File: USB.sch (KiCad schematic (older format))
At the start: 31 parts

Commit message: First version of schematics
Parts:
- added C30, C31, C33, C40, C41: 4u7, symbol device:C_Small
- added C34, C35, C36: 100n, symbol device:C_Small
- added C37, C38: 470u/6.3V, symbol device:CP_Small
- added C39: 1u, symbol device:C_Small
- added C42, C43: 22p, symbol device:C_Small
- added J4: Headphones, symbol conn:Audio-Jack-3
- added J5: Mic, symbol conn:Audio-Jack-3
- added R29: 1k5, symbol device:R_Small
- added R30, R31: 22, symbol device:R_Small
- added R32: 2k2, symbol device:R_Small
- added R33: 1k2, symbol device:R_Small
- added R34: 1M, symbol device:R_Small
- added U8: CM108, symbol GiantKnob:CM108
- added Y3: 12 MHz, symbol device:Crystal_Small
- gave numbers to parts that had none: 31
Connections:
- net +5V: now also C30.1, C31.1, C34.1, C35.1, C36.1, U8.29 (AVDD1), U8.34 (AVDD2), U8.35 (DVDD), U8.7 (PWRSEL)
- net GND: now also C30.2, C31.2, C33.1, C34.2, C35.2, C36.2, C40.2, C41.2, C42.1, C43.1, J4.3, J5.3, U8.10 (MODE), U8.14 (DVSS1), U8.16 (SDIN), U8.22 (ADSEL), U8.23 (TEST), U8.24 (AVSS1), U8.28 (VSEL), U8.33 (AVSS2), U8.36 (DVSS2), U8.38 (MSEL)
- net USBDM_AUDIO: now also R30.2
- net USBDP_AUDIO: now also R29.1, R31.2
- new net: R32.1, U8.25 (VBIAS)
- new net: C40.1, U8.26 (VREF)
- new net: C39.2, U8.27 (MICIN)
- new net: C38.1, U8.30 (LOL)
- new net: C37.1, U8.32 (LOR)
- new net: C33.2, R29.2, U8.37 (REGV)
- new net: R31.1, U8.41 (USBDP)
- new net: R30.1, U8.42 (USBDM)
- new net: C42.2, R34.1, U8.8 (XI), Y3.1
- new net: C43.2, R34.2, U8.9 (XO), Y3.2
- new net: C41.1, R32.2, R33.1
- new net: J5.2, R33.2
- new net: C39.1, J5.1
- new net: C38.2, J4.1
- new net: C37.2, J4.2
- no-connect marks 13 -> 37

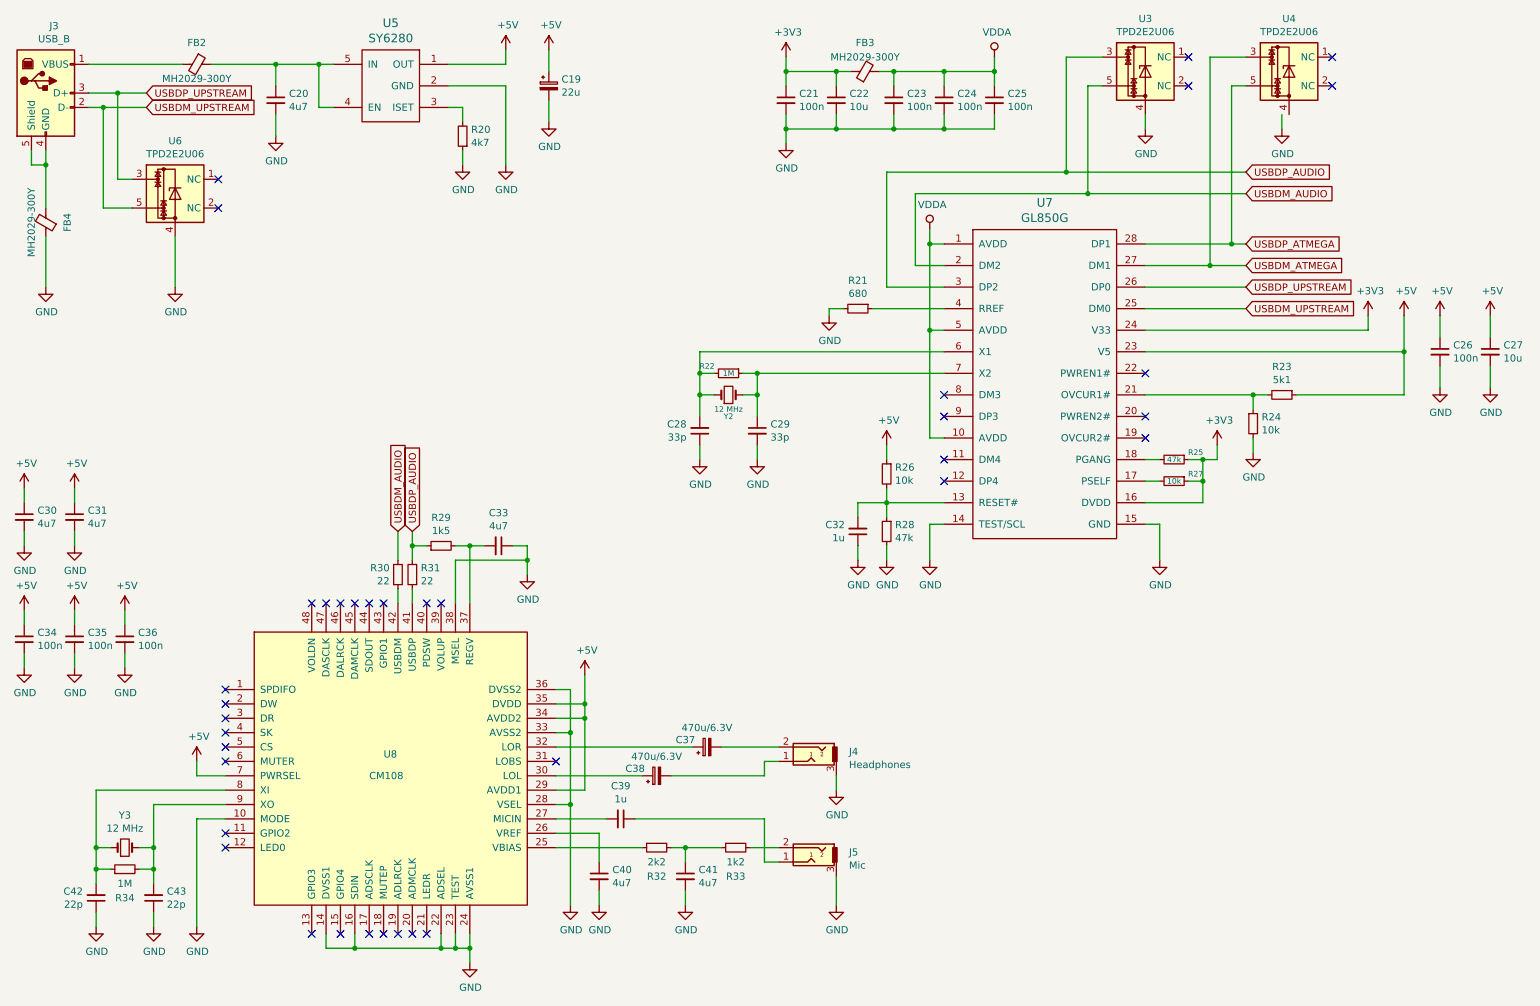
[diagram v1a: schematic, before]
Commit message: Added PTT to ATmega32U4
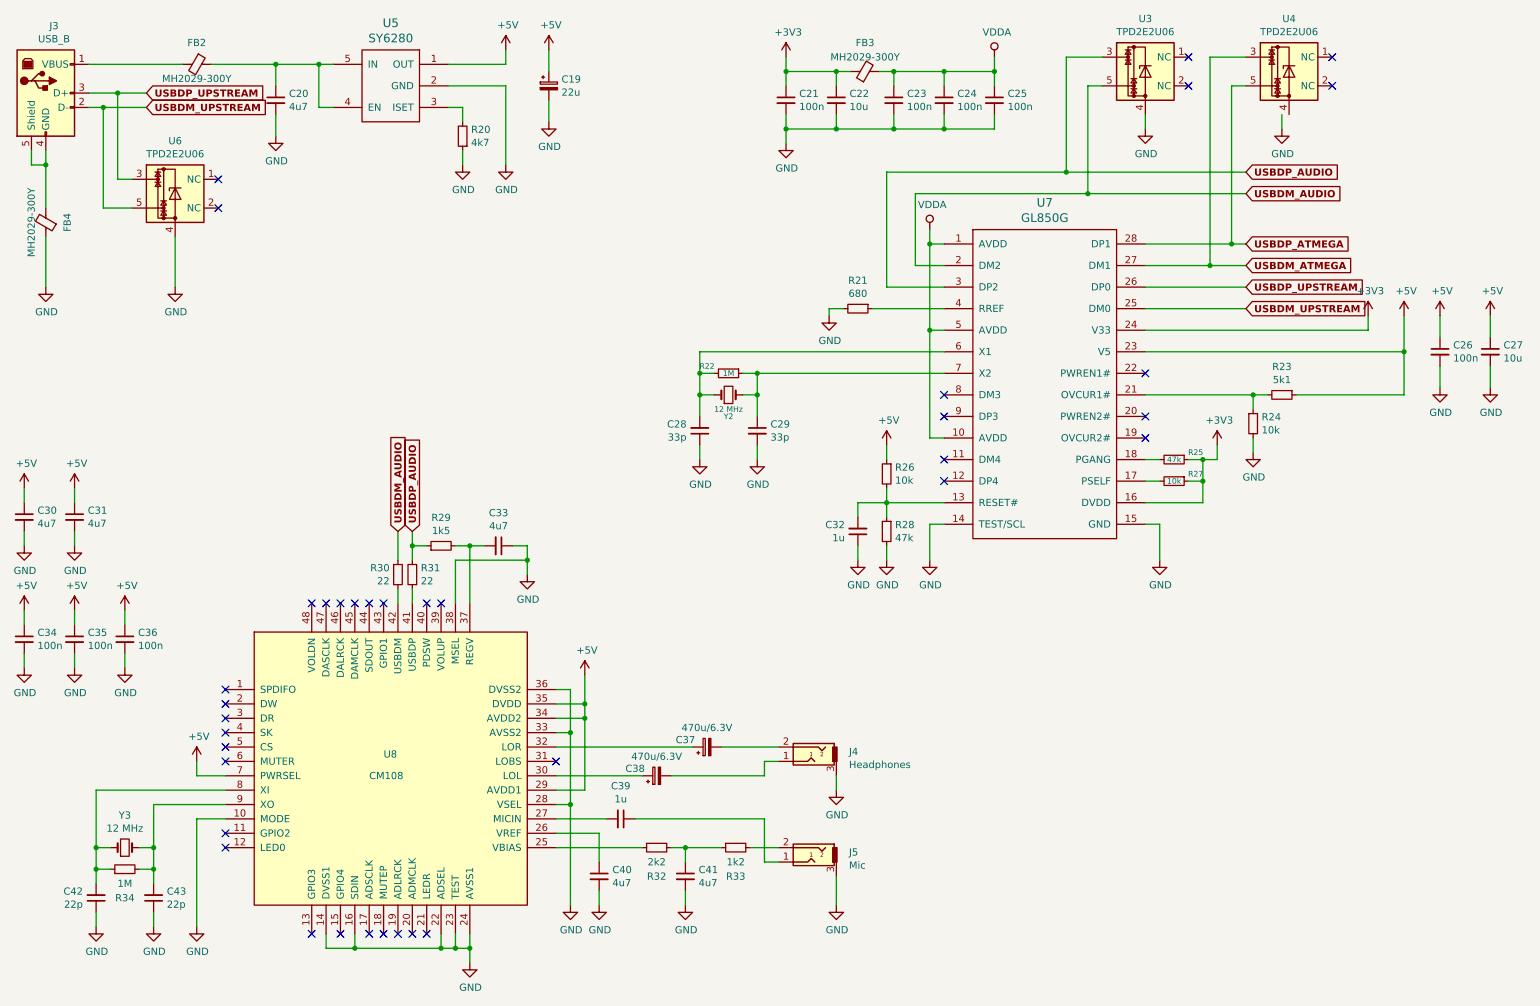
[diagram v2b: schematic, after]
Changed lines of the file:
@@
 Wire Wire Line
 	8500 1250 8500 1350
-Text GLabel 9200 1800 2    50   Input ~ 0
+Text GLabel 9200 1800 2    50   Input ~ 6
 USBDM_AUDIO
-Text GLabel 9200 1650 2    50   Input ~ 0
+Text GLabel 9200 1650 2    50   Input ~ 6
 USBDP_AUDIO
-Text GLabel 9200 2300 2    50   Input ~ 0
+Text GLabel 9200 2300 2    50   Input ~ 6
 USBDM_ATMEGA
-Text GLabel 9200 2150 2    50   Input ~ 0
+Text GLabel 9200 2150 2    50   Input ~ 6
 USBDP_ATMEGA
 Wire Wire Line
@@
 	1250 1200 1550 1200
 Connection ~ 1250 1200
-Text GLabel 1550 1100 2    50   Input ~ 0
+Text GLabel 1550 1100 2    50   Input ~ 6
 USBDP_UPSTREAM
-Text GLabel 1550 1200 2    50   Input ~ 0
+Text GLabel 1550 1200 2    50   Input ~ 6
 USBDM_UPSTREAM
-Text GLabel 9200 2450 2    50   Input ~ 0
+Text GLabel 9200 2450 2    50   Input ~ 6
 USBDP_UPSTREAM
-Text GLabel 9200 2600 2    50   Input ~ 0
+Text GLabel 9200 2600 2    50   Input ~ 6
 USBDM_UPSTREAM
 Wire Wire Line
@@
 Wire Wire Line
 	4200 4350 4200 4450
-Text GLabel 3400 4150 1    50   Input ~ 0
+Text GLabel 3400 4150 1    50   Input ~ 6
 USBDP_AUDIO
 Wire Wire Line
 	3400 4250 3400 4150
 Connection ~ 3400 4250
-Text GLabel 3300 4150 1    50   Input ~ 0
+Text GLabel 3300 4150 1    50   Input ~ 6
 USBDM_AUDIO
 Wire Wire Line

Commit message: Added component footprints
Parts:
- removed J3: USB_B, symbol GiantKnob-rescue:USB_B-Connector
- added J3: USB_B, Connectors:USB_Mini-B, symbol conn:USB_OTG
- C19: footprint (none) -> Capacitors_Tantalum_SMD:CP_Tantalum_Case-A_EIA-3216-18_Reflow
- C20, C21, C22, C23, C24, C25, C26, C27, C28, C29, C30, C31, C32, C33, C34, C35, C36, C39, C40, C41, C42, C43: footprint (none) -> Capacitors_SMD:C_0603
- C37, C38: footprint (none) -> Capacitors_Tantalum_SMD:CP_Tantalum_Case-D_EIA-7343-31_Reflow
- FB2, FB3, FB4: footprint (none) -> Inductors_SMD:L_0805
- J4, J5: footprint (none) -> GiantKnob:PJ-320B; LCSC (none) -> PJ-320B
- R20, R21, R22, R23, R24, R25, R26, R27, R28, R29, R30, R31, R32, R33, R34: footprint (none) -> Resistors_SMD:R_0603
- U3, U4, U6: footprint Package_TO_SOT_SMD:SOT-543 -> TO_SOT_Packages_SMD:SOT-543
- U5: footprint (none) -> TO_SOT_Packages_SMD:SOT-23-5
- U7: footprint (none) -> Housings_SSOP:SSOP-28_5.3x10.2mm_Pitch0.65mm
- U8: footprint (none) -> Housings_QFP:LQFP-48_7x7mm_Pitch0.5mm
- Y2, Y3: footprint (none) -> Crystals:Crystal_SMD_5032-2pin_5.0x3.2mm
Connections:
- net USBDM_UPSTREAM: now also J3.2 (D-)
- net USBDP_UPSTREAM: now also J3.3 (D+)
- net at FB2.2: now also J3.1 (VBUS)
- net at FB4.2: now also J3.5 (GND), J3.6 (Shield)
- no-connect marks 37 -> 38

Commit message: Board layout for prototype
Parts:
- removed U3, U4: TPD2E2U06, TO_SOT_Packages_SMD:SOT-543, symbol GiantKnob-rescue:TPD2E2U06-Power_Protection
- C19: footprint Capacitors_Tantalum_SMD:CP_Tantalum_Case-A_EIA-3216-18_Reflow -> Capacitor_Tantalum_SMD:CP_EIA-3216-18_Kemet-A
- C20, C21, C22, C23, C24, C25, C26, C27, C28, C29: footprint Capacitors_SMD:C_0603 -> Capacitor_SMD:C_0603_1608Metric
- C30, C31, C32, C33, C34, C35, C36, C39, C40, C41, C42, C43: footprint Capacitors_SMD:C_0603 -> Capacitor_SMD:C_0603_1608Metric; symbol device:C_Small -> GiantKnob-rescue:C_Small-device
- C37, C38: footprint Capacitors_Tantalum_SMD:CP_Tantalum_Case-D_EIA-7343-31_Reflow -> Capacitor_Tantalum_SMD:CP_EIA-7343-31_Kemet-D; symbol device:CP_Small -> GiantKnob-rescue:CP_Small-device
- FB2, FB3, FB4: footprint Inductors_SMD:L_0805 -> Inductor_SMD:L_0805_2012Metric
- J3: footprint Connectors:USB_Mini-B -> Connector_USB:USB_Mini-B_Lumberg_2486_01_Horizontal; symbol conn:USB_OTG -> GiantKnob-rescue:USB_OTG-conn
- J4, J5: symbol conn:Audio-Jack-3 -> GiantKnob-rescue:Audio-Jack-3-conn
- R20, R21, R23, R24, R25, R26, R27, R28, R29, R30, R31, R32, R33, R34: footprint Resistors_SMD:R_0603 -> Resistor_SMD:R_0603_1608Metric; symbol device:R_Small -> GiantKnob-rescue:R_Small-device
- R22: footprint Resistors_SMD:R_0603 -> Resistor_SMD:R_0603_1608Metric
- U5: footprint TO_SOT_Packages_SMD:SOT-23-5 -> Package_TO_SOT_SMD:SOT-23-5
- U6: footprint TO_SOT_Packages_SMD:SOT-543 -> Package_TO_SOT_SMD:SOT-553
- U7: footprint Housings_SSOP:SSOP-28_5.3x10.2mm_Pitch0.65mm -> Package_SO:SSOP-28_5.3x10.2mm_P0.65mm
- U8: footprint Housings_QFP:LQFP-48_7x7mm_Pitch0.5mm -> Package_QFP:LQFP-48_7x7mm_P0.5mm
- Y2: footprint Crystals:Crystal_SMD_5032-2pin_5.0x3.2mm -> Crystal:Crystal_SMD_5032-2Pin_5.0x3.2mm
- Y3: footprint Crystals:Crystal_SMD_5032-2pin_5.0x3.2mm -> Crystal:Crystal_SMD_5032-2Pin_5.0x3.2mm; symbol device:Crystal_Small -> GiantKnob-rescue:Crystal_Small-device
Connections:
- no-connect marks 38 -> 34
